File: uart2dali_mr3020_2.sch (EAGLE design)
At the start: 78 parts, among them IC2 LM393D, IC3 SFH6156, IC4 SFH6156, J1 AVR_SPI_PRG_6NS, Q1 SST201, Q2 BSP170P, Q3 BC817-25SMD, X1 SM04B-SRSS-TB

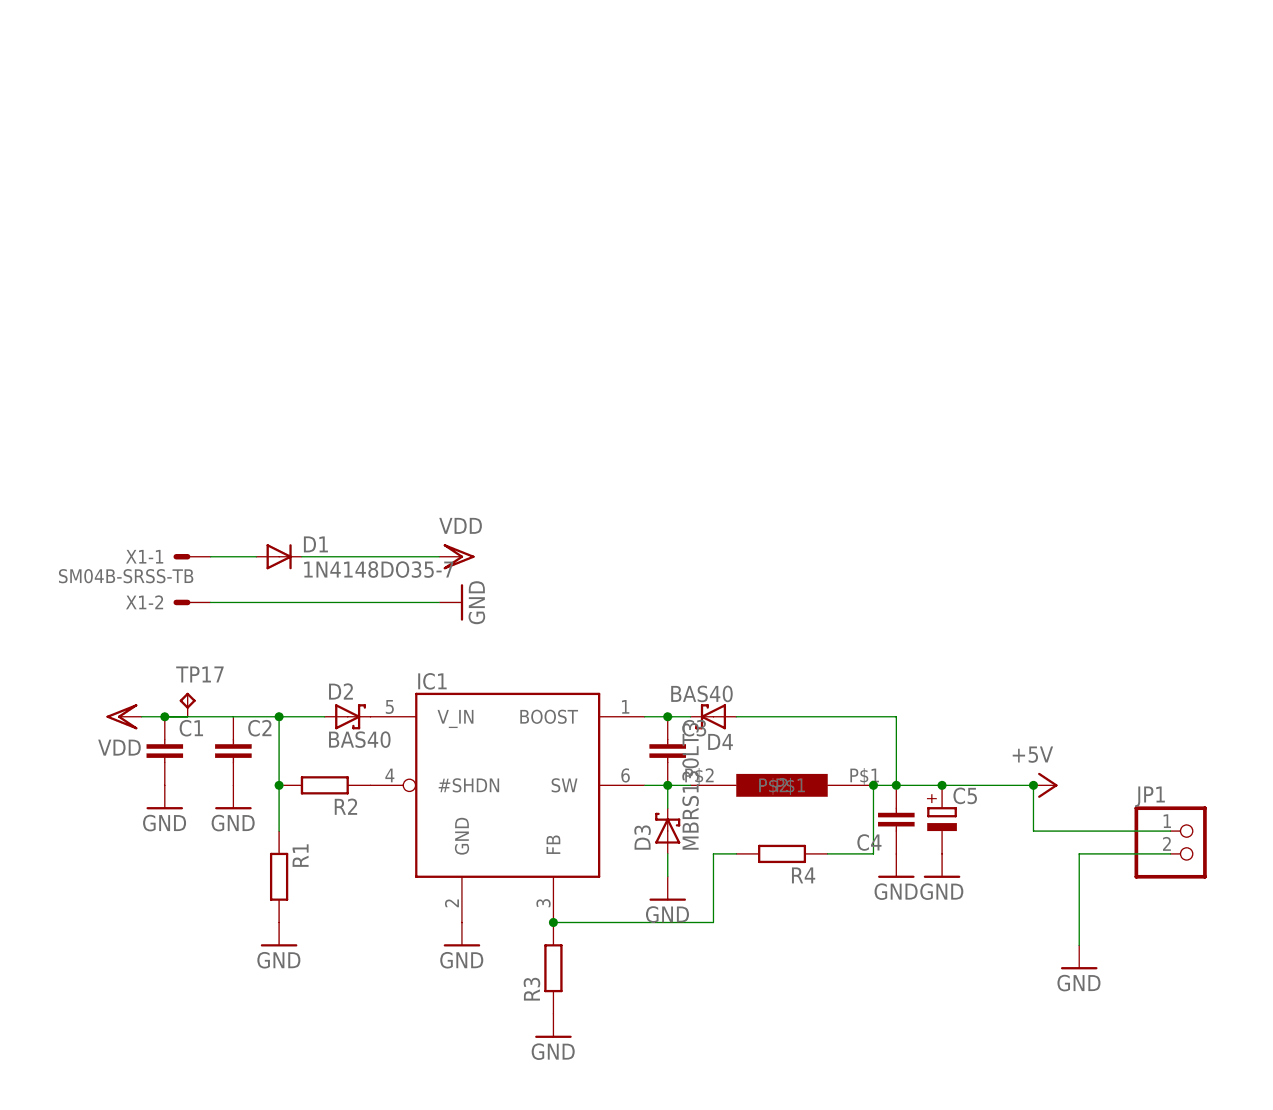
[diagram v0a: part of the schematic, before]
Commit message: new version of the base board with 2 switching regulators
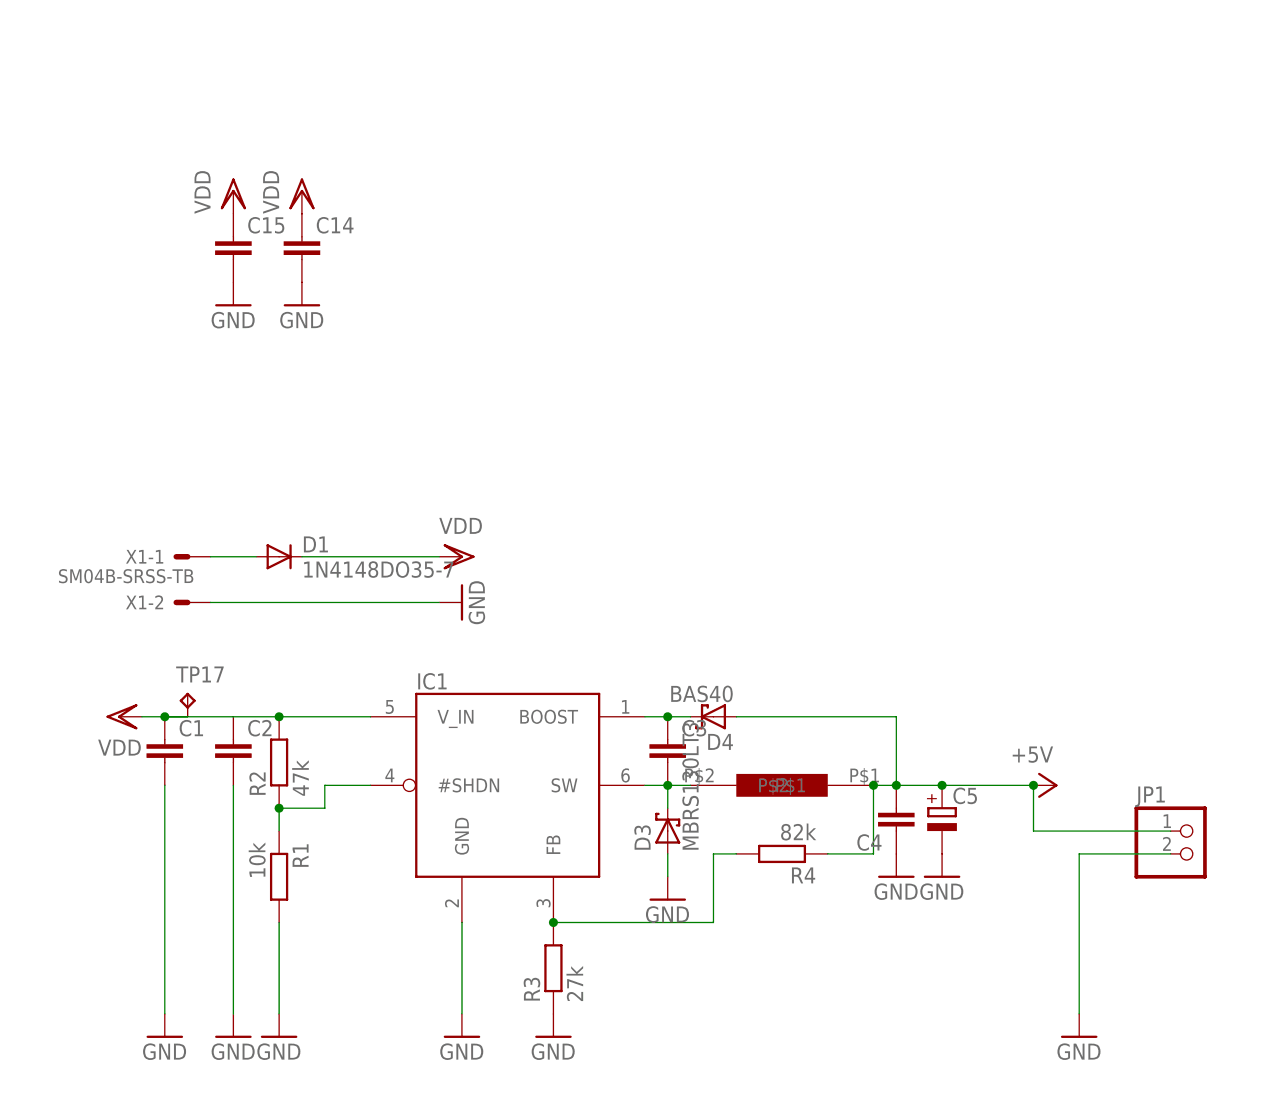
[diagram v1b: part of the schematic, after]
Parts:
- removed D2: BAS40, diode:BAS40
- added C14, C15: (no value), resistor:C-EUC0805
- R1: value (none) -> 10k
- R2: value (none) -> 47k
- R3: value (none) -> 27k
- R4: value (none) -> 82k
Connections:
- removed net N$18: IC1.#SHDN, R2.1
- net GND: now also C14.2, C15.2
- net N$3: now also IC1.#SHDN, R1.1, R2.1; no longer D2.C, IC1.V_IN
- net VDD: now also C14.1, C15.1, IC1.V_IN; no longer D2.A, R1.1
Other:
- moved on the sheet: R2
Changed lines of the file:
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@@
 <part name="U$1" library="inductor" deviceset="KMP_2330_UNSHIELDED" device=""/>
 <part name="U$3" library="inductor" deviceset="SDR0805" device=""/>
-<part name="D2" library="diode" deviceset="BAS40" device=""/>
 <part name="D3" library="diode" deviceset="MBRS130LT3" device=""/>
 <part name="D4" library="diode" deviceset="BAS40" device=""/>
-<part name="R2" library="resistor" deviceset="R-EU_" device="R0603"/>
-<part name="R1" library="resistor" deviceset="R-EU_" device="R0603"/>
+<part name="R2" library="resistor" deviceset="R-EU_" device="R0603" value="47k"/>
+<part name="R1" library="resistor" deviceset="R-EU_" device="R0603" value="10k"/>
 <part name="GND4" library="supply1" deviceset="GND" device=""/>
 <part name="C3" library="resistor" deviceset="C-EU" device="C0805"/>
 <part name="GND13" library="supply1" deviceset="GND" device=""/>
-<part name="R3" library="resistor" deviceset="R-EU_" device="R0603"/>
-<part name="R4" library="resistor" deviceset="R-EU_" device="R0603"/>
+<part name="R3" library="resistor" deviceset="R-EU_" device="R0603" value="27k"/>
+<part name="R4" library="resistor" deviceset="R-EU_" device="R0603" value="82k"/>
 <part name="GND23" library="supply1" deviceset="GND" device=""/>
 <part name="P+13" library="supply1" deviceset="VCC/2" device=""/>
@@
 <part name="C13" library="resistor" deviceset="C-EU" device="C0805"/>
 <part name="GND27" library="supply1" deviceset="GND" device=""/>
+<part name="C14" library="resistor" deviceset="C-EU" device="C0805"/>
+<part name="C15" library="resistor" deviceset="C-EU" device="C0805"/>
+<part name="GND18" library="supply1" deviceset="GND" device=""/>
+<part name="GND32" library="supply1" deviceset="GND" device=""/>
+<part name="VDD5" library="supply1" deviceset="VDD" device=""/>
+<part name="VDD6" library="supply1" deviceset="VDD" device=""/>
 </parts>
 <sheets>
@@
 <instance part="VDD4" gate="G$1" x="5.08" y="58.42" rot="R90"/>
 <instance part="C1" gate="G$1" x="10.16" y="55.88"/>
-<instance part="GND14" gate="1" x="10.16" y="48.26"/>
+<instance part="GND14" gate="1" x="10.16" y="22.86"/>
 <instance part="C2" gate="G$1" x="17.78" y="55.88"/>
-<instance part="GND15" gate="1" x="17.78" y="48.26"/>
+<instance part="GND15" gate="1" x="17.78" y="22.86"/>
 <instance part="C4" gate="G$1" x="91.44" y="45.72" rot="R180"/>
 <instance part="GND16" gate="1" x="91.44" y="40.64"/>
@@
 <instance part="X1" gate="-4" x="487.68" y="109.22" rot="R180"/>
 <instance part="JP1" gate="G$1" x="124.46" y="43.18"/>
-<instance part="GND5" gate="1" x="111.76" y="30.48"/>
+<instance part="GND5" gate="1" x="111.76" y="22.86"/>
 <instance part="U$2" gate="G$1" x="228.6" y="63.5"/>
 <instance part="P+6" gate="1" x="215.9" y="109.22"/>
@@
 <instance part="P+12" gate="G$1" x="518.16" y="106.68" rot="R90"/>
 <instance part="IC1" gate="G$1" x="48.26" y="50.8"/>
-<instance part="GND1" gate="1" x="43.18" y="33.02"/>
+<instance part="GND1" gate="1" x="43.18" y="22.86"/>
 <instance part="U$1" gate="G$1" x="78.74" y="50.8" rot="R180"/>
 <instance part="U$3" gate="G$1" x="436.88" y="68.58" rot="R90"/>
-<instance part="D2" gate="1" x="30.48" y="58.42"/>
 <instance part="D3" gate="G$1" x="66.04" y="45.72" rot="R90"/>
 <instance part="D4" gate="1" x="71.12" y="58.42" rot="R180"/>
-<instance part="R2" gate="G$1" x="27.94" y="50.8" rot="R180"/>
+<instance part="R2" gate="G$1" x="22.86" y="53.34" rot="R90"/>
 <instance part="R1" gate="G$1" x="22.86" y="40.64" rot="R270"/>
-<instance part="GND4" gate="1" x="22.86" y="33.02"/>
+<instance part="GND4" gate="1" x="22.86" y="22.86"/>
 <instance part="C3" gate="G$1" x="66.04" y="55.88"/>
 <instance part="GND13" gate="1" x="66.04" y="38.1"/>
@@
 <instance part="C13" gate="G$1" x="444.5" y="50.8" rot="R180"/>
 <instance part="GND27" gate="1" x="444.5" y="45.72"/>
+<instance part="C14" gate="G$1" x="25.4" y="111.76"/>
+<instance part="C15" gate="G$1" x="17.78" y="111.76"/>
+<instance part="GND18" gate="1" x="25.4" y="104.14"/>
+<instance part="GND32" gate="1" x="17.78" y="104.14"/>
+<instance part="VDD5" gate="G$1" x="17.78" y="116.84"/>
+<instance part="VDD6" gate="G$1" x="25.4" y="116.84"/>
 </instances>
 <busses>
@@
 <pinref part="C1" gate="G$1" pin="2"/>
 <pinref part="GND14" gate="1" pin="GND"/>
+<wire x1="10.16" y1="25.4" x2="10.16" y2="50.8" width="0.1524" layer="91"/>
 </segment>
 <segment>
 <pinref part="C2" gate="G$1" pin="2"/>
 <pinref part="GND15" gate="1" pin="GND"/>
+<wire x1="17.78" y1="25.4" x2="17.78" y2="50.8" width="0.1524" layer="91"/>
 </segment>
 <segment>
@@
 <pinref part="JP1" gate="G$1" pin="2"/>
 <wire x1="121.92" y1="43.18" x2="111.76" y2="43.18" width="0.1524" layer="91"/>
-<wire x1="111.76" y1="43.18" x2="111.76" y2="33.02" width="0.1524" layer="91"/>
+<wire x1="111.76" y1="43.18" x2="111.76" y2="25.4" width="0.1524" layer="91"/>
 <pinref part="GND5" gate="1" pin="GND"/>
 </segment>
@@
 <pinref part="IC1" gate="G$1" pin="GND"/>
 <pinref part="GND1" gate="1" pin="GND"/>
+<wire x1="43.18" y1="25.4" x2="43.18" y2="35.56" width="0.1524" layer="91"/>
 </segment>
 <segment>
 <pinref part="R1" gate="G$1" pin="2"/>
 <pinref part="GND4" gate="1" pin="GND"/>
+<wire x1="22.86" y1="25.4" x2="22.86" y2="35.56" width="0.1524" layer="91"/>
 </segment>
 <segment>
@@
 <pinref part="C13" gate="G$1" pin="1"/>
 <pinref part="GND27" gate="1" pin="GND"/>
+</segment>
+<segment>
+<pinref part="C14" gate="G$1" pin="2"/>
+<pinref part="GND18" gate="1" pin="GND"/>
+</segment>
+<segment>
+<pinref part="C15" gate="G$1" pin="2"/>
+<pinref part="GND32" gate="1" pin="GND"/>
 </segment>
 </net>
@@
 <pinref part="TP17" gate="G$1" pin="TP"/>
 <wire x1="10.16" y1="58.42" x2="12.7" y2="58.42" width="0.1524" layer="91"/>
-<pinref part="R1" gate="G$1" pin="1"/>
 <pinref part="R2" gate="G$1" pin="2"/>
-<wire x1="22.86" y1="45.72" x2="22.86" y2="50.8" width="0.1524" layer="91"/>
-<wire x1="22.86" y1="50.8" x2="22.86" y2="58.42" width="0.1524" layer="91"/>
 <wire x1="22.86" y1="58.42" x2="17.78" y2="58.42" width="0.1524" layer="91"/>
-<pinref part="D2" gate="1" pin="A"/>
-<wire x1="27.94" y1="58.42" x2="22.86" y2="58.42" width="0.1524" layer="91"/>
 <junction x="22.86" y="58.42"/>
-<junction x="22.86" y="50.8"/>
+<pinref part="IC1" gate="G$1" pin="V_IN"/>
+<wire x1="33.02" y1="58.42" x2="22.86" y2="58.42" width="0.1524" layer="91"/>
 </segment>
 <segment>
@@
 <junction x="436.88" y="106.68"/>
 </segment>
+<segment>
+<pinref part="C15" gate="G$1" pin="1"/>
+<pinref part="VDD5" gate="G$1" pin="VDD"/>
+</segment>
+<segment>
+<pinref part="C14" gate="G$1" pin="1"/>
+<pinref part="VDD6" gate="G$1" pin="VDD"/>
+</segment>
 </net>
 <net name="N$19" class="0">
@@
 <wire x1="444.5" y1="43.18" x2="408.94" y2="43.18" width="0.1524" layer="91"/>
 <pinref part="R17" gate="G$1" pin="1"/>
-</segment>
-</net>
-<net name="N$3" class="0">
-<segment>
-<pinref part="IC1" gate="G$1" pin="V_IN"/>
-<pinref part="D2" gate="1" pin="C"/>
-</segment>
-</net>
-<net name="N$18" class="0">
-<segment>
-<pinref part="IC1" gate="G$1" pin="#SHDN"/>
-<pinref part="R2" gate="G$1" pin="1"/>
 </segment>
 </net>
@@
 </segment>
 </net>
+<net name="N$3" class="0">
+<segment>
+<pinref part="R2" gate="G$1" pin="1"/>
+<pinref part="R1" gate="G$1" pin="1"/>
+<wire x1="22.86" y1="48.26" x2="22.86" y2="45.72" width="0.1524" layer="91"/>
+<pinref part="IC1" gate="G$1" pin="#SHDN"/>
+<wire x1="33.02" y1="50.8" x2="27.94" y2="50.8" width="0.1524" layer="91"/>
+<wire x1="27.94" y1="50.8" x2="27.94" y2="48.26" width="0.1524" layer="91"/>
+<wire x1="27.94" y1="48.26" x2="22.86" y2="48.26" width="0.1524" layer="91"/>
+<junction x="22.86" y="48.26"/>
+</segment>
+</net>

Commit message: - fixed mispelling in dali_encode - added dali_encode to SConstruct - minor fixes on schematics and board
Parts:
- D11: value BZX84CSMD -> BZX84CSMD 2V7
- R24: value (none) -> 4R7
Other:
- moved on the sheet: R4, TP10
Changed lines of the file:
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@@
 <part name="Q3" library="transistor-npn" deviceset="BC817*" device="SMD" technology="-25"/>
 <part name="D10" library="diode" deviceset="BAS40" device=""/>
-<part name="D11" library="diode" deviceset="BZX84CSMD" device=""/>
+<part name="D11" library="diode" deviceset="BZX84CSMD" device="" value="BZX84CSMD 2V7"/>
 <part name="D9" library="diode" deviceset="BZX85" device=""/>
 <part name="R25" library="resistor" deviceset="R-EU_" device="R0603"/>
 <part name="R23" library="resistor" deviceset="R-EU_" device="R0603"/>
-<part name="R24" library="resistor" deviceset="R-EU_" device="R0603"/>
+<part name="R24" library="resistor" deviceset="R-EU_" device="R0603" value="4R7"/>
 <part name="R21" library="resistor" deviceset="R-EU_" device="R0603"/>
 <part name="R22" library="resistor" deviceset="R-EU_" device="R0603"/>
@@
 <instance part="GND15" gate="1" x="17.78" y="22.86"/>
 <instance part="C4" gate="G$1" x="91.44" y="45.72" rot="R180"/>
-<instance part="GND16" gate="1" x="91.44" y="40.64"/>
-<instance part="GND17" gate="1" x="96.52" y="40.64"/>
+<instance part="GND16" gate="1" x="91.44" y="22.86"/>
+<instance part="GND17" gate="1" x="96.52" y="22.86"/>
 <instance part="D1" gate="G$1" x="22.86" y="76.2"/>
 <instance part="P+9" gate="1" x="182.88" y="68.58" rot="R90"/>
@@
 <instance part="TP8" gate="G$1" x="236.22" y="147.32"/>
 <instance part="TP9" gate="G$1" x="226.06" y="22.86" rot="R180"/>
-<instance part="TP10" gate="G$1" x="177.8" y="76.2" rot="R90"/>
+<instance part="TP10" gate="G$1" x="182.88" y="76.2" rot="R90"/>
 <instance part="GND6" gate="1" x="314.96" y="38.1" rot="R90"/>
 <instance part="P+7" gate="1" x="314.96" y="43.18" rot="R270"/>
@@
 <instance part="GND4" gate="1" x="22.86" y="22.86"/>
 <instance part="C3" gate="G$1" x="66.04" y="55.88"/>
-<instance part="GND13" gate="1" x="66.04" y="38.1"/>
+<instance part="GND13" gate="1" x="66.04" y="40.64"/>
 <instance part="R3" gate="G$1" x="53.34" y="30.48" rot="R90"/>
-<instance part="R4" gate="G$1" x="78.74" y="43.18" rot="R180"/>
+<instance part="R4" gate="G$1" x="78.74" y="35.56" rot="R180"/>
 <instance part="GND23" gate="1" x="53.34" y="22.86"/>
 <instance part="P+13" gate="G$1" x="449.58" y="58.42" rot="R270"/>
@@
 <pinref part="TP10" gate="G$1" pin="TP"/>
 <pinref part="U$2" gate="G$1" pin="PD3"/>
-<wire x1="180.34" y1="76.2" x2="200.66" y2="76.2" width="0.1524" layer="91"/>
-<label x="180.34" y="76.2" size="1.778" layer="95"/>
+<wire x1="185.42" y1="76.2" x2="200.66" y2="76.2" width="0.1524" layer="91"/>
+<label x="185.42" y="76.2" size="1.778" layer="95"/>
 </segment>
 <segment>
@@
 <pinref part="C4" gate="G$1" pin="1"/>
 <pinref part="GND16" gate="1" pin="GND"/>
+<wire x1="91.44" y1="25.4" x2="91.44" y2="43.18" width="0.1524" layer="91"/>
 </segment>
 <segment>
 <pinref part="GND17" gate="1" pin="GND"/>
 <pinref part="C5" gate="G$1" pin="-"/>
+<wire x1="96.52" y1="25.4" x2="96.52" y2="43.18" width="0.1524" layer="91"/>
 </segment>
 <segment>
@@
 <pinref part="D3" gate="G$1" pin="A"/>
 <pinref part="GND13" gate="1" pin="GND"/>
-<wire x1="66.04" y1="43.18" x2="66.04" y2="40.64" width="0.1524" layer="91"/>
 </segment>
 <segment>
@@
 <wire x1="91.44" y1="50.8" x2="88.9" y2="50.8" width="0.1524" layer="91"/>
 <pinref part="R4" gate="G$1" pin="1"/>
-<wire x1="83.82" y1="43.18" x2="88.9" y2="43.18" width="0.1524" layer="91"/>
-<wire x1="88.9" y1="43.18" x2="88.9" y2="50.8" width="0.1524" layer="91"/>
+<wire x1="83.82" y1="35.56" x2="88.9" y2="35.56" width="0.1524" layer="91"/>
+<wire x1="88.9" y1="35.56" x2="88.9" y2="50.8" width="0.1524" layer="91"/>
 <junction x="88.9" y="50.8"/>
 </segment>
@@
 <pinref part="R4" gate="G$1" pin="2"/>
 <pinref part="R4" gate="G$1" pin="2"/>
-<wire x1="73.66" y1="43.18" x2="71.12" y2="43.18" width="0.1524" layer="91"/>
-<wire x1="71.12" y1="43.18" x2="71.12" y2="35.56" width="0.1524" layer="91"/>
-<wire x1="71.12" y1="35.56" x2="53.34" y2="35.56" width="0.1524" layer="91"/>
+<wire x1="73.66" y1="35.56" x2="53.34" y2="35.56" width="0.1524" layer="91"/>
 <junction x="53.34" y="35.56"/>
 </segment>
